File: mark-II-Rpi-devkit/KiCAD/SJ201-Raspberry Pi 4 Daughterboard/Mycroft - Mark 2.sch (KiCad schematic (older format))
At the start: 7 parts

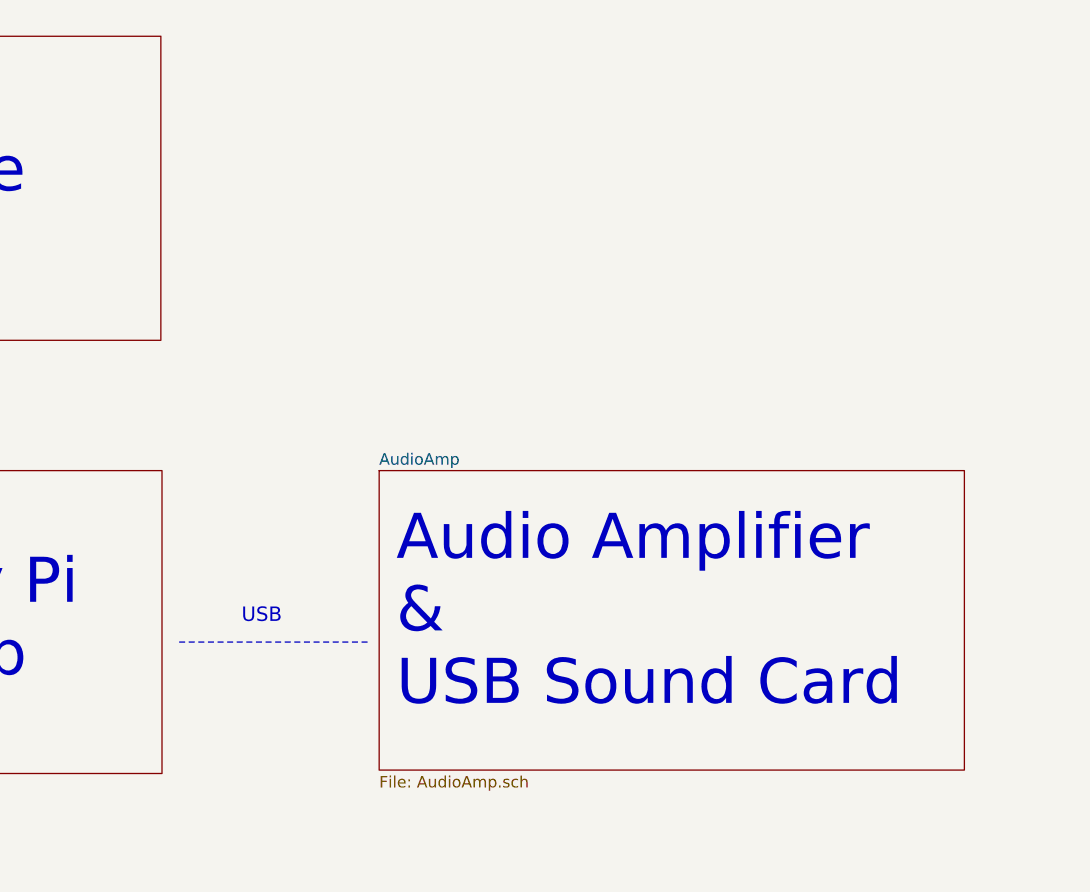
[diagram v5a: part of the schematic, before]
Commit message: SJ201 - Removed CM108b soundcard, added in I2S to Line out, ATTin402. Moved holes in layout. SJ202 - extened length to plug into USB2.0 port
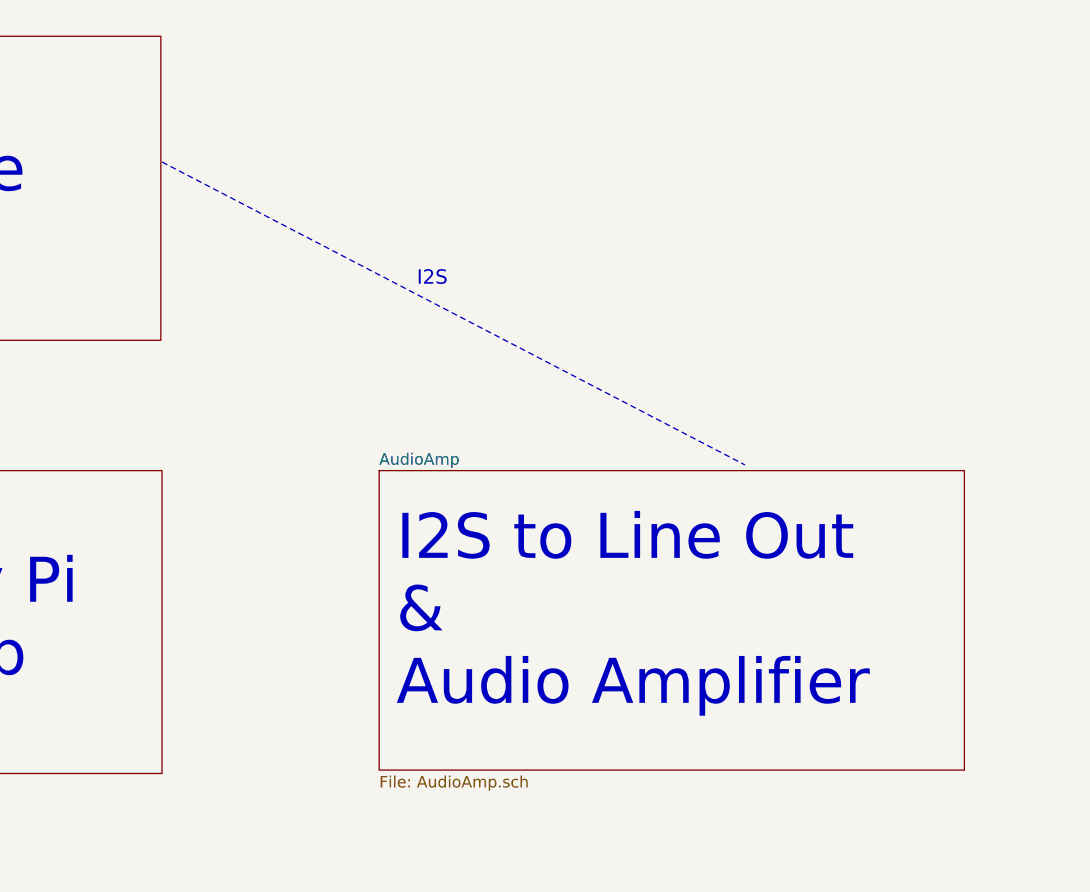
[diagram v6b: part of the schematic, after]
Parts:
- H1, H2, H3, H4: footprint MountingHole:MountingHole_3mm_Pad_Via -> MountingHole:MountingHole_3mm_Pad; MPN (none) -> DNP
- H5, H6, H7: MPN (none) -> DNP
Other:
- note added: "I2S"
- note added: "I2S to Line Out\n&\nAudio Amplifier\n"
- note removed: "Audio Amplifier\n& \nUSB Sound Card"
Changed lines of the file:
@@
 Sheet 1 6
 Title ""
-Date "2020-08-16"
-Rev "0.66"
+Date "2020-09-26"
+Rev "0.67b"
 Comp "Mycroft"
 Comment1 ""
@@
 Raspberry Pi\n& USB Hub
 Text Notes 7575 3900 0    197  ~ 0
-Audio Amplifier\n& \nUSB Sound Card
+I2S to Line Out\n&\nAudio Amplifier\n
 Text Notes 4375 1975 0    197  ~ 0
 XMOS\nMicrophone \nArray
@@
 Wire Notes Line
 	5690 2835 5690 2335
-Text Notes 7075 3525 2    63   ~ 0
-USB
+Text Notes 7800 2050 2    63   ~ 0
+I2S
 Wire Notes Line
-	6625 3600 7450 3600
+	6550 1500 9100 2825
 $Comp
 L Mechanical:MountingHole H1
@@
 F 0 "H1" H 8100 6146 50  0000 L CNN
 F 1 "MountingHole" H 8100 6055 50  0000 L CNN
-F 2 "MountingHole:MountingHole_3mm_Pad_Via" H 8000 6100 50  0001 C CNN
+F 2 "MountingHole:MountingHole_3mm_Pad" H 8000 6100 50  0001 C CNN
 F 3 "~" H 8000 6100 50  0001 C CNN
+F 4 "DNP" H 8000 6100 50  0001 C CNN "MPN"
 	1    8000 6100
 	1    0    0    -1
@@
 F 0 "H2" H 8100 6321 50  0000 L CNN
 F 1 "MountingHole" H 8100 6230 50  0000 L CNN
-F 2 "MountingHole:MountingHole_3mm_Pad_Via" H 8000 6275 50  0001 C CNN
+F 2 "MountingHole:MountingHole_3mm_Pad" H 8000 6275 50  0001 C CNN
 F 3 "~" H 8000 6275 50  0001 C CNN
+F 4 "DNP" H 8000 6275 50  0001 C CNN "MPN"
 	1    8000 6275
 	1    0    0    -1
@@
 F 0 "H3" H 8100 6521 50  0000 L CNN
 F 1 "MountingHole" H 8100 6430 50  0000 L CNN
-F 2 "MountingHole:MountingHole_3mm_Pad_Via" H 8000 6475 50  0001 C CNN
+F 2 "MountingHole:MountingHole_3mm_Pad" H 8000 6475 50  0001 C CNN
 F 3 "~" H 8000 6475 50  0001 C CNN
+F 4 "DNP" H 8000 6475 50  0001 C CNN "MPN"
 	1    8000 6475
 	1    0    0    -1
@@
 F 0 "H4" H 8100 6721 50  0000 L CNN
 F 1 "MountingHole" H 8100 6630 50  0000 L CNN
-F 2 "MountingHole:MountingHole_3mm_Pad_Via" H 8000 6675 50  0001 C CNN
+F 2 "MountingHole:MountingHole_3mm_Pad" H 8000 6675 50  0001 C CNN
 F 3 "~" H 8000 6675 50  0001 C CNN
+F 4 "DNP" H 8000 6675 50  0001 C CNN "MPN"
 	1    8000 6675
 	1    0    0    -1
@@
 F 2 "mycroft:mycroft_logo_graphic" H 8800 6650 50  0001 C CNN
 F 3 "~" H 8800 6650 50  0001 C CNN
+F 4 "DNP" H 8800 6650 50  0001 C CNN "MPN"
 	1    8800 6650
 	1    0    0    -1
@@
 F 2 "Symbol:OSHW-Symbol_6.7x6mm_SilkScreen" H 8800 6475 50  0001 C CNN
 F 3 "~" H 8800 6475 50  0001 C CNN
+F 4 "DNP" H 8800 6475 50  0001 C CNN "MPN"
 	1    8800 6475
 	1    0    0    -1
@@
 F 2 "mycroft:mycroft_logo_words" H 8975 6650 50  0001 C CNN
 F 3 "~" H 8975 6650 50  0001 C CNN
+F 4 "DNP" H 8975 6650 50  0001 C CNN "MPN"
 	1    8975 6650
 	1    0    0    -1
